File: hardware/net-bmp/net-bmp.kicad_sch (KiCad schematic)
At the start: 27 parts, among them J1 DBG, J2 Micro SD, SW1 SW_SPST, U1 STM32F407VETx

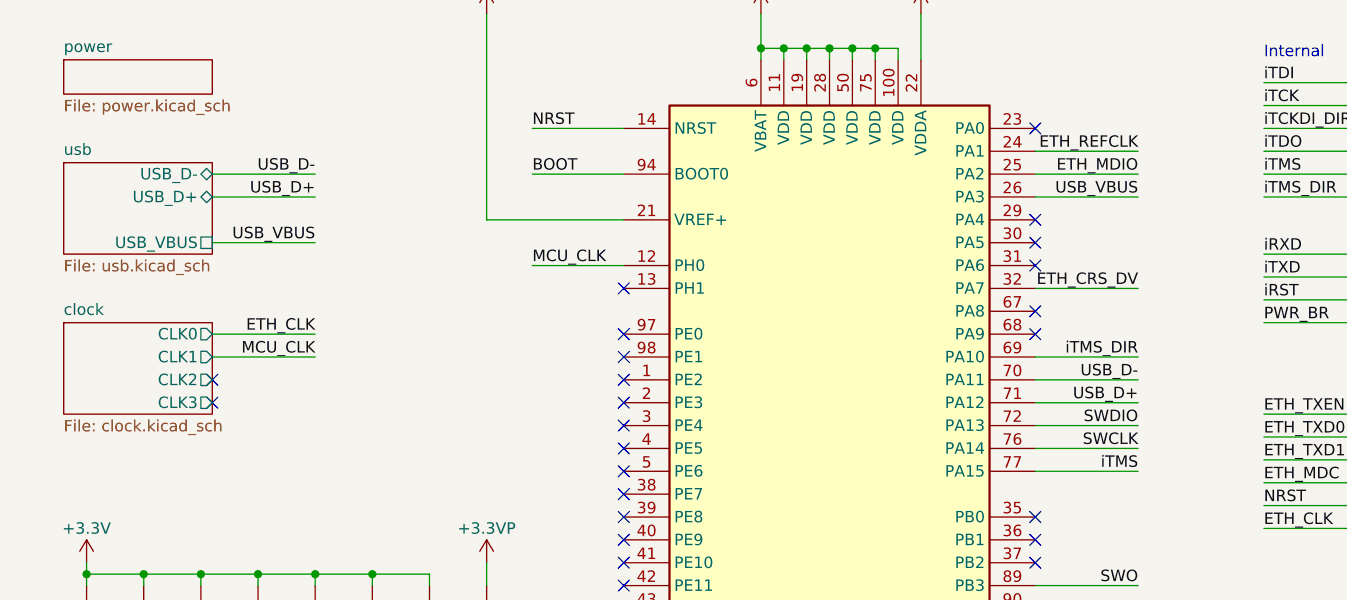
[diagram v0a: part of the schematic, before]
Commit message: chore: build with stubs
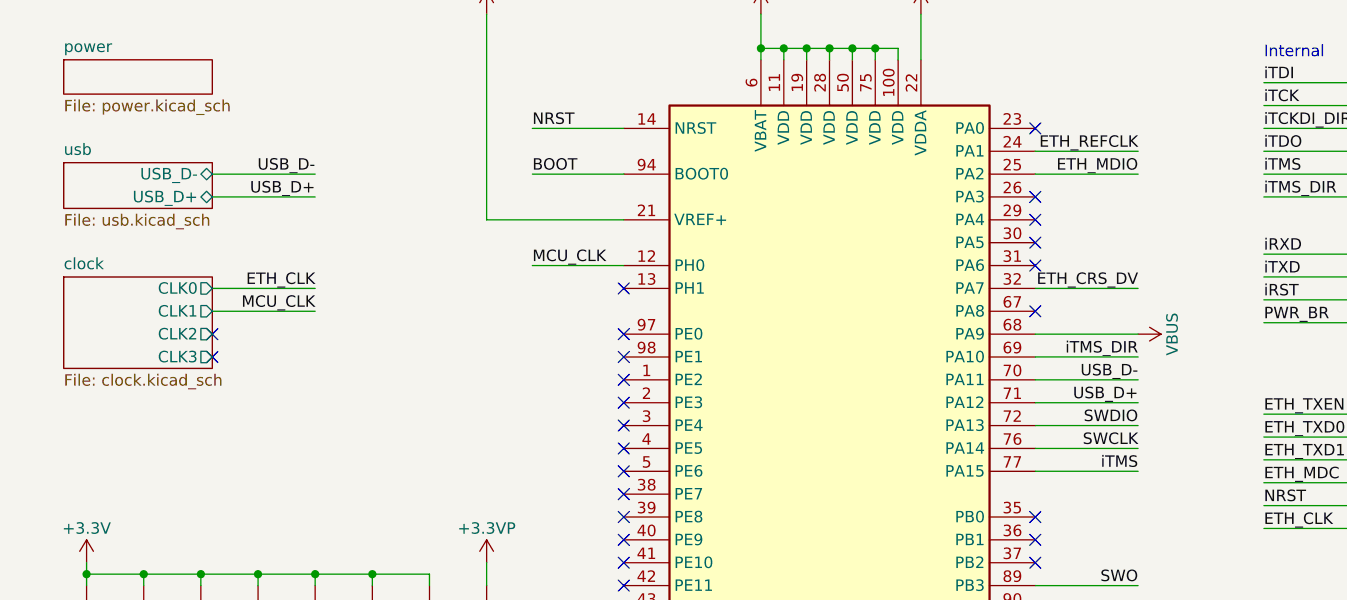
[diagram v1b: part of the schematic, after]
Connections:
- net VBUS: now reaches U1.68 (PA9)
- net USB_VBUS: no longer names the net of U1.26 (PA3)
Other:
- sheet usb ports: added none; removed USB_VBUS
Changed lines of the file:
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@@
   (title_block
     (title "net-bmp")
-    (date "2023-10-31")
-    (rev "a")
+    (date "2023-11-11")
+    (rev "b")
     (company "elagil")
   )
@@
   (no_connect (at 137.16 52.07))
   (no_connect (at 91.44 80.01))
-  (no_connect (at 137.16 64.77))
+  (no_connect (at 137.16 49.53))
   (no_connect (at 91.44 102.87))
   (no_connect (at 177.8 113.03))
@@
   (no_connect (at 137.16 87.63))
   (no_connect (at 137.16 143.51))
-  (no_connect (at 45.72 69.85))
+  (no_connect (at 45.72 64.77))
   (no_connect (at 91.44 115.57))
   (no_connect (at 91.44 90.17))
@@
   (no_connect (at 91.44 74.93))
   (no_connect (at 137.16 161.29))
-  (no_connect (at 45.72 72.39))
+  (no_connect (at 45.72 67.31))
   (no_connect (at 177.8 130.81))
   (no_connect (at 137.16 163.83))
@@
     (stroke (width 0) (type default))
   )
-  (wire (pts (xy 45.72 64.77) (xy 57.15 64.77))
+  (wire (pts (xy 45.72 59.69) (xy 57.15 59.69))
     (stroke (width 0) (type default))
   )
@@
     (stroke (width 0) (type default))
   )
-  (wire (pts (xy 45.72 67.31) (xy 57.15 67.31))
+  (wire (pts (xy 45.72 62.23) (xy 57.15 62.23))
     (stroke (width 0) (type default))
   )
@@
     (stroke (width 0) (type default))
   )
-  (wire (pts (xy 137.16 49.53) (xy 148.59 49.53))
-    (stroke (width 0) (type default))
-  )
   (wire (pts (xy 237.49 137.16) (xy 243.84 137.16))
     (stroke (width 0) (type default))
@@
     (stroke (width 0) (type default))
   )
-  (wire (pts (xy 45.72 54.61) (xy 57.15 54.61))
-    (stroke (width 0) (type default))
-  )
   (wire (pts (xy 69.85 100.33) (xy 69.85 104.14))
     (stroke (width 0) (type default))
@@
     (stroke (width 0) (type default))
   )
+  (wire (pts (xy 137.16 64.77) (xy 148.59 64.77))
+    (stroke (width 0) (type default))
+  )
   (wire (pts (xy 45.72 49.53) (xy 57.15 49.53))
     (stroke (width 0) (type default))
@@
     (effects (font (size 1.27 1.27)) (justify right bottom))
   )
-  (label "MCU_CLK" (at 57.15 67.31 180) (fields_autoplaced)
+  (label "MCU_CLK" (at 57.15 62.23 180) (fields_autoplaced)
     (effects (font (size 1.27 1.27)) (justify right bottom))
   )
@@
     (effects (font (size 1.27 1.27)) (justify left bottom))
   )
-  (label "USB_VBUS" (at 57.15 54.61 180) (fields_autoplaced)
-    (effects (font (size 1.27 1.27)) (justify right bottom))
-  )
   (label "PWR_BR" (at 162.56 63.5 0) (fields_autoplaced)
     (effects (font (size 1.27 1.27)) (justify left bottom))
@@
     (effects (font (size 1.27 1.27)) (justify right bottom))
   )
-  (label "USB_VBUS" (at 148.59 49.53 180) (fields_autoplaced)
-    (effects (font (size 1.27 1.27)) (justify right bottom))
-  )
   (label "iRXD" (at 162.56 55.88 0) (fields_autoplaced)
     (effects (font (size 1.27 1.27)) (justify left bottom))
@@
     (effects (font (size 1.27 1.27)) (justify right bottom))
   )
-  (label "ETH_CLK" (at 57.15 64.77 180) (fields_autoplaced)
+  (label "ETH_CLK" (at 57.15 59.69 180) (fields_autoplaced)
     (effects (font (size 1.27 1.27)) (justify right bottom))
   )
@@
         (path "/0556e588-02fe-48e5-93e8-fa3aab1c90e7"
           (reference "#PWR011") (unit 1)
+        )
+      )
+    )
+  )
+  (symbol (lib_id "power:VBUS") (at 148.59 64.77 270) (unit 1)
+    (in_bom yes) (on_board yes) (dnp no)
+    (property "Reference" "#PWR067" (at 144.78 64.77 0)
+      (effects (font (size 1.27 1.27)) hide)
+    )
+    (property "Value" "VBUS" (at 152.4 64.77 0)
+      (effects (font (size 1.27 1.27)))
+    )
+    (property "Footprint" "" (at 148.59 64.77 0)
+      (effects (font (size 1.27 1.27)) hide)
+    )
+    (property "Datasheet" "" (at 148.59 64.77 0)
+      (effects (font (size 1.27 1.27)) hide)
+    )
+    (pin "1")
+    (instances
+      (project "net-bmp"
+        (path "/0556e588-02fe-48e5-93e8-fa3aab1c90e7/e157d64e-477b-4983-afb5-0491664aa612"
+          (reference "#PWR067") (unit 1)
+        )
+        (path "/0556e588-02fe-48e5-93e8-fa3aab1c90e7"
+          (reference "#PWR064") (unit 1)
         )
       )
@@
     )
   )
-  (sheet (at 29.21 63.5) (size 16.51 10.16) (fields_autoplaced)
+  (sheet (at 29.21 58.42) (size 16.51 10.16) (fields_autoplaced)
     (stroke (width 0.1524) (type solid))
     (fill (color 0 0 0 0.0000))
-    (property "Sheetname" "clock" (at 29.21 62.7884 0)
+    (property "Sheetname" "clock" (at 29.21 57.7084 0)
       (effects (font (size 1.27 1.27)) (justify left bottom))
     )
-    (property "Sheetfile" "clock.kicad_sch" (at 29.21 74.2446 0)
+    (property "Sheetfile" "clock.kicad_sch" (at 29.21 69.1646 0)
       (effects (font (size 1.27 1.27)) (justify left top))
     )
-    (pin "CLK1" output (at 45.72 67.31 0)
-      (effects (font (size 1.27 1.27)) (justify right))
-    )
-    (pin "CLK3" output (at 45.72 72.39 0)
-      (effects (font (size 1.27 1.27)) (justify right))
-    )
-    (pin "CLK0" output (at 45.72 64.77 0)
-      (effects (font (size 1.27 1.27)) (justify right))
-    )
-    (pin "CLK2" output (at 45.72 69.85 0)
+    (pin "CLK1" output (at 45.72 62.23 0)
+      (effects (font (size 1.27 1.27)) (justify right))
+    )
+    (pin "CLK3" output (at 45.72 67.31 0)
+      (effects (font (size 1.27 1.27)) (justify right))
+    )
+    (pin "CLK0" output (at 45.72 59.69 0)
+      (effects (font (size 1.27 1.27)) (justify right))
+    )
+    (pin "CLK2" output (at 45.72 64.77 0)
       (effects (font (size 1.27 1.27)) (justify right))
     )
@@
     )
   )
-  (sheet (at 29.21 45.72) (size 16.51 10.16) (fields_autoplaced)
+  (sheet (at 29.21 45.72) (size 16.51 5.08) (fields_autoplaced)
     (stroke (width 0.1524) (type solid))
     (fill (color 0 0 0 0.0000))
@@
       (effects (font (size 1.27 1.27)) (justify left bottom))
     )
-    (property "Sheetfile" "usb.kicad_sch" (at 29.21 56.4646 0)
+    (property "Sheetfile" "usb.kicad_sch" (at 29.21 51.3846 0)
       (effects (font (size 1.27 1.27)) (justify left top))
     )
@@
       (effects (font (size 1.27 1.27)) (justify right))
     )
-    (pin "USB_VBUS" passive (at 45.72 54.61 0)
-      (effects (font (size 1.27 1.27)) (justify right))
-    )
